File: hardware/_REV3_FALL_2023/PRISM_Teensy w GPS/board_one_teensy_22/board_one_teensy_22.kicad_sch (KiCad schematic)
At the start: 25 parts, among them J1 Micro_SD_Card_Det_Hirose_DM3AT, J3 3387, U1 Teensy4.0, U2 GPS-14414, U3 3966, U4 RFM69HCW_Breakout, U5 SFN-1407PA7.6

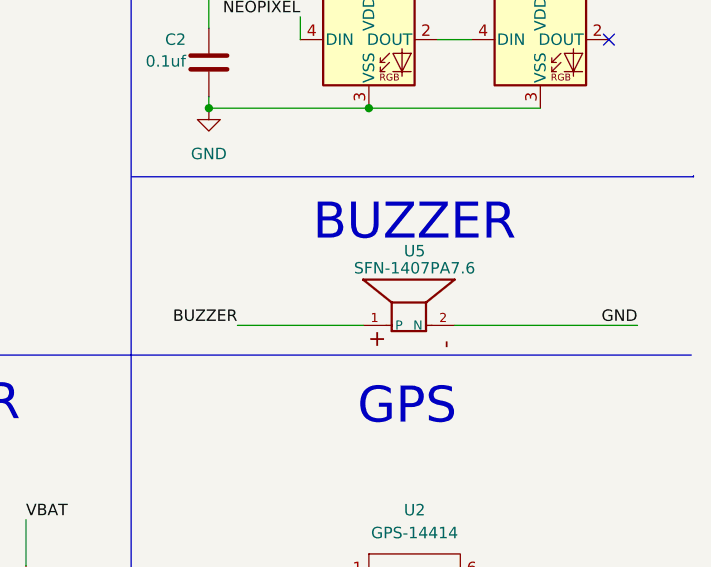
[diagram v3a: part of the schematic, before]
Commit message: Add big buzzer to FC
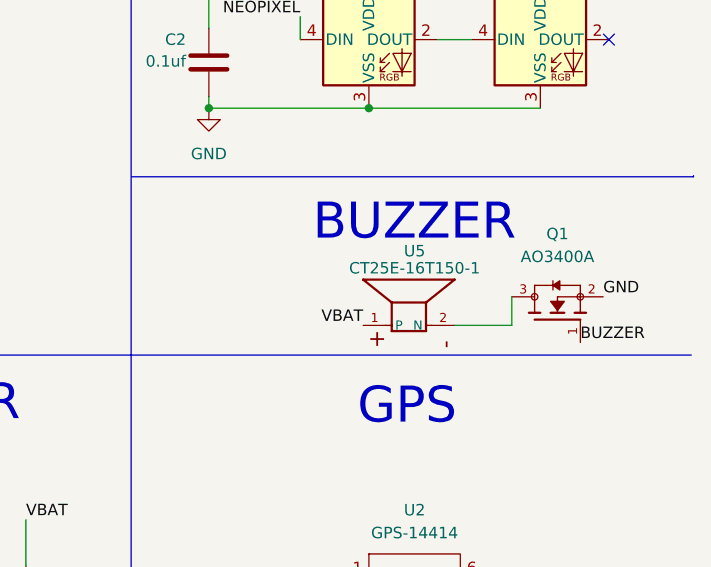
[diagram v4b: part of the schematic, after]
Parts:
- added Q1: AO3400A, rocketry_footprints:SOT95P280X125-3N, symbol AO3400A:AO3400A
- U5: value SFN-1407PA7.6 -> CT25E-16T150-1; footprint rocketry_footprints:SFN-1407PA7.6 -> rocketry_footprints:CT25E-16T150-1; Vendor C360603 -> (none)
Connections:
- net BUZZER: now also Q1.1; no longer U5.1 (P)
- net GND: now also Q1.2; no longer U5.2 (N)
- net VBAT: now also U5.1 (P)
- new net: Q1.3, U5.2 (N)
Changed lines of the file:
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@@
+    (stroke (width 0) (type default))
+  )
+  (wire (pts (xy 258.445 67.31) (xy 264.795 67.31))
     (stroke (width 0) (type default))
   )
@@
     (stroke (width 0) (type default))
   )
-  (wire (pts (xy 234.315 67.31) (xy 248.285 67.31))
-    (stroke (width 0) (type default))
-  )
   (wire (pts (xy 27.94 171.45) (xy 34.925 171.45))
     (stroke (width 0) (type default))
@@
     (stroke (width 0) (type default))
   )
-  (wire (pts (xy 258.445 67.31) (xy 278.765 67.31))
-    (stroke (width 0) (type default))
-  )
   (wire (pts (xy 135.255 186.69) (xy 144.145 186.69))
     (stroke (width 0) (type default))
@@
     (stroke (width 0) (type default))
   )
+  (wire (pts (xy 264.795 67.31) (xy 264.795 64.135))
+    (stroke (width 0) (type default))
+  )
   (polyline (pts (xy 222.504 128.905) (xy 222.504 70.612))
     (stroke (width 0) (type default))
@@
     (effects (font (size 1.27 1.27)) (justify right bottom))
   )
-  (label "BUZZER" (at 234.315 67.31 180) (fields_autoplaced)
-    (effects (font (size 1.27 1.27)) (justify right bottom))
+  (label "BUZZER" (at 272.415 69.215 0) (fields_autoplaced)
+    (effects (font (size 1.27 1.27)) (justify left bottom))
   )
   (label "GND" (at 182.88 30.48 180) (fields_autoplaced)
@@
     (effects (font (size 1.27 1.27)) (justify left bottom))
   )
-  (label "GND" (at 278.765 67.31 180) (fields_autoplaced)
-    (effects (font (size 1.27 1.27)) (justify right bottom))
+  (label "GND" (at 274.955 64.135 0) (fields_autoplaced)
+    (effects (font (size 1.27 1.27)) (justify left bottom))
   )
   (label "MOSI" (at 44.45 87.63 180) (fields_autoplaced)
@@
   (label "3.3V" (at 135.255 156.21 0) (fields_autoplaced)
     (effects (font (size 1.27 1.27)) (justify left bottom))
+  )
+  (label "VBAT" (at 248.285 67.31 180) (fields_autoplaced)
+    (effects (font (size 1.27 1.27)) (justify right bottom))
   )
   (label "V_Mon" (at 186.69 99.06 180) (fields_autoplaced)
@@
     )
   )
+  (symbol (lib_id "AO3400A:AO3400A") (at 269.875 66.675 90) (unit 1)
+    (in_bom yes) (on_board yes) (dnp no) (fields_autoplaced)
+    (property "Reference" "Q1" (at 269.875 57.15 90)
+      (effects (font (size 1.27 1.27)))
+    )
+    (property "Value" "AO3400A" (at 269.875 59.69 90)
+      (effects (font (size 1.27 1.27)))
+    )
+    (property "Footprint" "rocketry_footprints:SOT95P280X125-3N" (at 269.875 66.675 0)
+      (effects (font (size 1.27 1.27)) (justify bottom) hide)
+    )
+    (property "Datasheet" "" (at 269.875 66.675 0)
+      (effects (font (size 1.27 1.27)) hide)
+    )
+    (property "STANDARD" "IPC 7351B" (at 269.875 66.675 0)
+      (effects (font (size 1.27 1.27)) (justify bottom) hide)
+    )
+    (property "MAXIMUM_PACKAGE_HEIGHT" "1.25 mm" (at 269.875 66.675 0)
+      (effects (font (size 1.27 1.27)) (justify bottom) hide)
+    )
+    (property "MANUFACTURER" "Alpha & Omega Semiconductor" (at 269.875 66.675 0)
+      (effects (font (size 1.27 1.27)) (justify bottom) hide)
+    )
+    (property "PARTREV" "L" (at 269.875 66.675 0)
+      (effects (font (size 1.27 1.27)) (justify bottom) hide)
+    )
+    (property "Vendor" "C20917" (at 269.875 66.675 0)
+      (effects (font (size 1.27 1.27)) hide)
+    )
+    (pin "1")
+    (pin "2")
+    (pin "3")
+    (instances
+      (project "board_one_teensy_22"
+        (path "/7a48c3b0-2761-409e-ae2f-7ebae3820225"
+          (reference "Q1") (unit 1)
+        )
+      )
+      (project "CoreIO"
+        (path "/9e212ca8-0a67-4365-b4eb-6661fcc83758"
+          (reference "Q1") (unit 1)
+        )
+      )
+    )
+  )
   (symbol (lib_id "SMT-0827-S-HT-R:SMT-0827-S-HT-R") (at 253.365 64.77 90) (unit 1)
     (in_bom yes) (on_board yes) (dnp no)
@@
       (effects (font (size 1.27 1.27)))
     )
-    (property "Value" "SFN-1407PA7.6" (at 254 60.96 90)
+    (property "Value" "CT25E-16T150-1" (at 254 60.96 90)
       (effects (font (size 1.27 1.27)))
     )
-    (property "Footprint" "rocketry_footprints:SFN-1407PA7.6" (at 253.365 64.77 0)
+    (property "Footprint" "rocketry_footprints:CT25E-16T150-1" (at 253.365 64.77 0)
       (effects (font (size 1.27 1.27)) (justify bottom) hide)
     )
@@
       (effects (font (size 1.27 1.27)) (justify bottom) hide)
     )
-    (property "Vendor" "C360603" (at 253.365 64.77 90)
-      (effects (font (size 1.27 1.27)) hide)
-    )
     (pin "1")

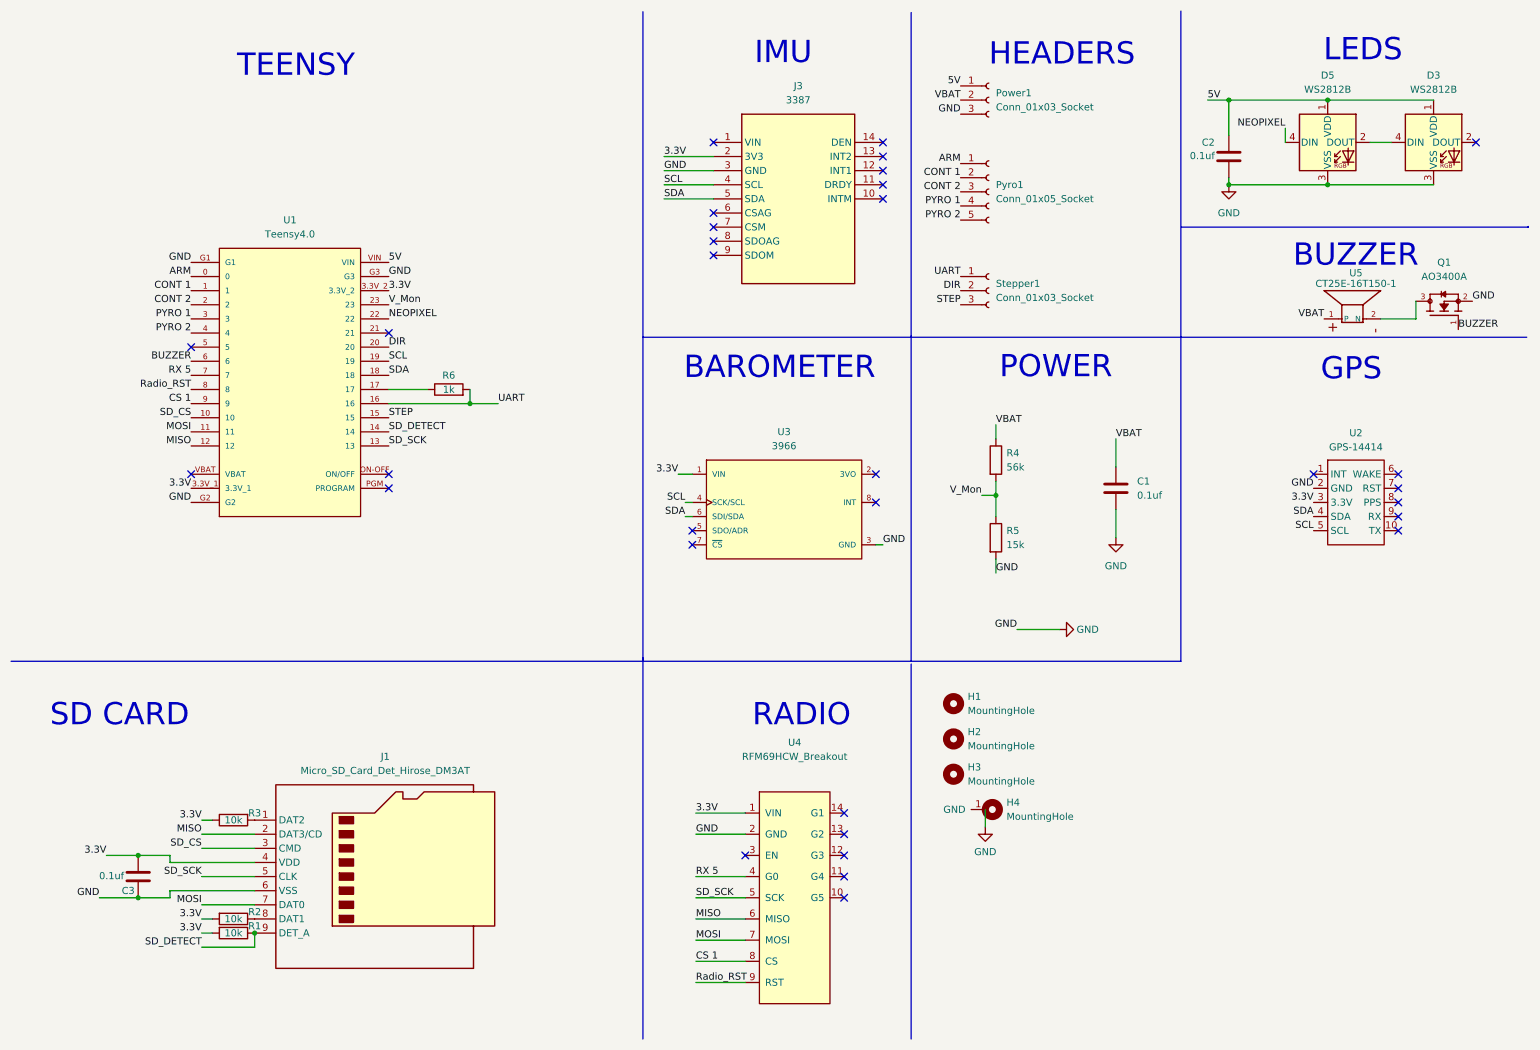
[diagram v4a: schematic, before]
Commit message: Add two buzzers to FC
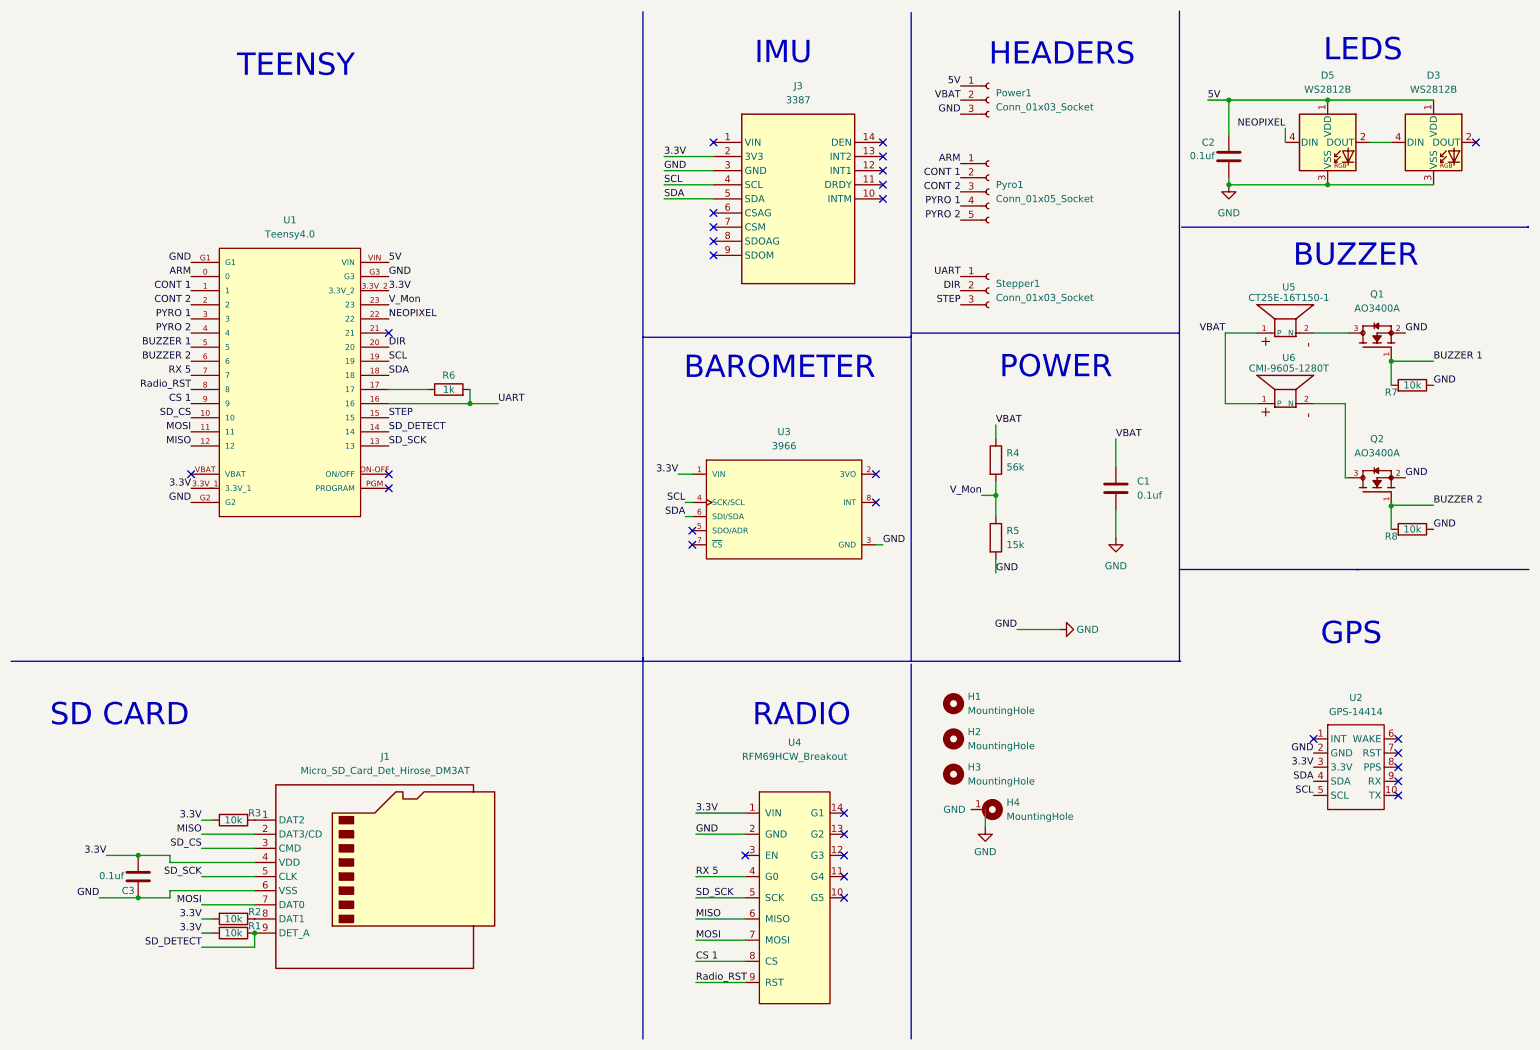
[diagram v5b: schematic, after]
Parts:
- added Q2: AO3400A, rocketry_footprints:SOT95P280X125-3N, symbol AO3400A:AO3400A
- added R7, R8: 10k, Resistor_SMD:R_0603_1608Metric_Pad0.98x0.95mm_HandSolder, symbol Device:R
- added U6: CMI-9605-1280T, rocketry_footprints:CMI-9605-1280T, symbol SMT-0827-S-HT-R:SMT-0827-S-HT-R
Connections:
- net GND: now also Q2.2, R7.1, R8.1
- net VBAT: now also U6.1 (P)
- net BUZZER 1: now reaches U1.5
- net BUZZER 1: now also Q1.1, R7.2
- net BUZZER renamed BUZZER 2
- net BUZZER 2: now also Q2.1, R8.2; no longer Q1.1
- new net: Q2.3, U6.2 (N)
- no-connect marks 32 -> 31
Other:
- moved on the sheet: Q1, U2, U5

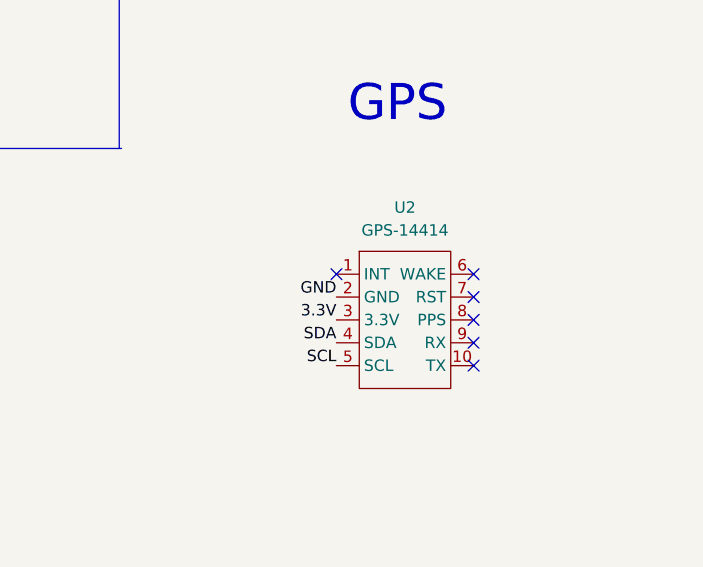
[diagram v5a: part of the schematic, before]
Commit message: Fixed GPS breakout schematic pin assignment and updated board to update traces
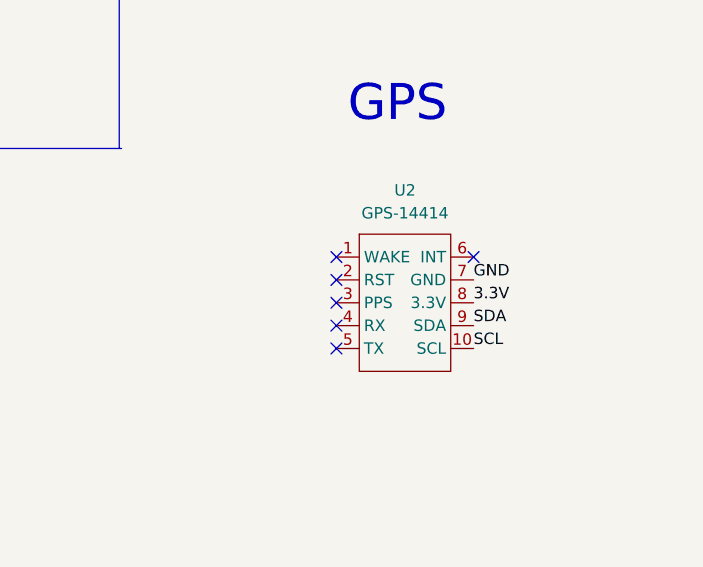
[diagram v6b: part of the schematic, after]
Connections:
- net 3.3V: now also U2.8 (3.3V); no longer U2.3 (3.3V)
- net GND: now also U2.7 (GND); no longer U2.2 (GND)
- net SCL: now also U2.10 (SCL); no longer U2.5 (SCL)
- net SDA: now also U2.9 (SDA); no longer U2.4 (SDA)
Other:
- moved on the sheet: U2
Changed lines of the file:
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@@
   (junction (at 231.14 43.18) (diameter 0) (color 0 0 0 0)
   )
-  (no_connect (at 261.62 147.955))
+  (no_connect (at 261.62 140.97))
   (no_connect (at 168.91 38.1))
   (no_connect (at 144.145 163.83))
   (no_connect (at 161.925 167.64))
   (no_connect (at 275.59 35.56))
-  (no_connect (at 261.62 153.035))
   (no_connect (at 44.45 95.25))
-  (no_connect (at 246.38 142.875))
+  (no_connect (at 246.38 151.13))
+  (no_connect (at 246.38 140.97))
   (no_connect (at 161.925 156.21))
   (no_connect (at 80.01 69.85))
@@
   (no_connect (at 134.62 107.95))
   (no_connect (at 80.01 95.25))
+  (no_connect (at 246.38 143.51))
   (no_connect (at 80.01 97.79))
   (no_connect (at 168.91 43.18))
@@
   (no_connect (at 168.91 40.64))
   (no_connect (at 168.91 45.72))
+  (no_connect (at 246.38 148.59))
   (no_connect (at 138.43 48.26))
-  (no_connect (at 261.62 142.875))
   (no_connect (at 161.925 163.83))
   (no_connect (at 168.91 35.56))
   (no_connect (at 138.43 55.88))
   (no_connect (at 138.43 53.34))
-  (no_connect (at 261.62 145.415))
+  (no_connect (at 246.38 146.05))
   (no_connect (at 138.43 35.56))
-  (no_connect (at 261.62 150.495))
   (no_connect (at 138.43 50.8))
   (wire (pts (xy 135.255 175.26) (xy 144.145 175.26))
@@
     (effects (font (size 1.27 1.27)) (justify left bottom))
   )
+  (label "SCL" (at 261.62 151.13 0) (fields_autoplaced)
+    (effects (font (size 1.27 1.27)) (justify left bottom))
+  )
   (label "3.3V" (at 29.21 163.83 180) (fields_autoplaced)
     (effects (font (size 1.27 1.27)) (justify right bottom))
@@
     (effects (font (size 1.27 1.27)) (justify right bottom))
   )
-  (label "3.3V" (at 246.38 147.955 180) (fields_autoplaced)
-    (effects (font (size 1.27 1.27)) (justify right bottom))
-  )
   (label "GND" (at 262.89 95.885 0) (fields_autoplaced)
     (effects (font (size 1.27 1.27)) (justify left bottom))
   )
-  (label "SDA" (at 246.38 150.495 180) (fields_autoplaced)
-    (effects (font (size 1.27 1.27)) (justify right bottom))
-  )
   (label "SD_CS" (at 44.45 85.09 180) (fields_autoplaced)
     (effects (font (size 1.27 1.27)) (justify right bottom))
@@
     (effects (font (size 1.27 1.27)) (justify right bottom))
   )
-  (label "SCL" (at 246.38 153.035 180) (fields_autoplaced)
-    (effects (font (size 1.27 1.27)) (justify right bottom))
-  )
   (label "STEP" (at 80.01 85.09 0) (fields_autoplaced)
     (effects (font (size 1.27 1.27)) (justify left bottom))
@@
     (effects (font (size 1.27 1.27)) (justify left bottom))
   )
+  (label "GND" (at 261.62 143.51 0) (fields_autoplaced)
+    (effects (font (size 1.27 1.27)) (justify left bottom))
+  )
   (label "BUZZER 1" (at 267.97 74.93 0) (fields_autoplaced)
     (effects (font (size 1.27 1.27)) (justify left bottom))
@@
     (effects (font (size 1.27 1.27)) (justify left bottom))
   )
+  (label "3.3V" (at 261.62 146.05 0) (fields_autoplaced)
+    (effects (font (size 1.27 1.27)) (justify left bottom))
+  )
   (label "DIR" (at 80.01 72.39 0) (fields_autoplaced)
     (effects (font (size 1.27 1.27)) (justify left bottom))
@@
     (effects (font (size 1.27 1.27)) (justify left bottom))
   )
-  (label "GND" (at 246.38 145.415 180) (fields_autoplaced)
-    (effects (font (size 1.27 1.27)) (justify right bottom))
-  )
   (label "RX 5" (at 135.255 167.64 0) (fields_autoplaced)
     (effects (font (size 1.27 1.27)) (justify left bottom))
@@
   (label "PYRO 2" (at 44.45 69.85 180) (fields_autoplaced)
     (effects (font (size 1.27 1.27)) (justify right bottom))
+  )
+  (label "SDA" (at 261.62 148.59 0) (fields_autoplaced)
+    (effects (font (size 1.27 1.27)) (justify left bottom))
   )
   (label "CS 1" (at 44.45 82.55 180) (fields_autoplaced)
@@
     )
   )
-  (symbol (lib_name "GPS-14414_1") (lib_id "GPS:GPS-14414") (at 254 144.145 0) (unit 1)
+  (symbol (lib_id "GPS:GPS-14414") (at 254 142.24 0) (unit 1)
     (in_bom yes) (on_board yes) (dnp no) (fields_autoplaced)
-    (property "Reference" "U2" (at 254 135.461 0)
-      (effects (font (size 1.27 1.27)))
-    )
-    (property "Value" "GPS-14414" (at 254 138.001 0)
-      (effects (font (size 1.27 1.27)))
-    )
-    (property "Footprint" "rocketry_footprints:GPS-14414" (at 254 144.145 0)
-      (effects (font (size 1.27 1.27)) hide)
-    )
-    (property "Datasheet" "" (at 254 144.145 0)
-      (effects (font (size 1.27 1.27)) hide)
-    )
+    (property "Reference" "U2" (at 254 133.556 0)
+      (effects (font (size 1.27 1.27)))
+    )
+    (property "Value" "GPS-14414" (at 254 136.096 0)
+      (effects (font (size 1.27 1.27)))
+    )
+    (property "Footprint" "rocketry_footprints:GPS-14414" (at 254 142.24 0)
+      (effects (font (size 1.27 1.27)) hide)
+    )
+    (property "Datasheet" "" (at 254 142.24 0)
+      (effects (font (size 1.27 1.27)) hide)
+    )
